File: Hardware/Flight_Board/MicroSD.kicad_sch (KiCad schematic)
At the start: 14 parts, among them J5 MEM2067-02-180-00-A_REVB

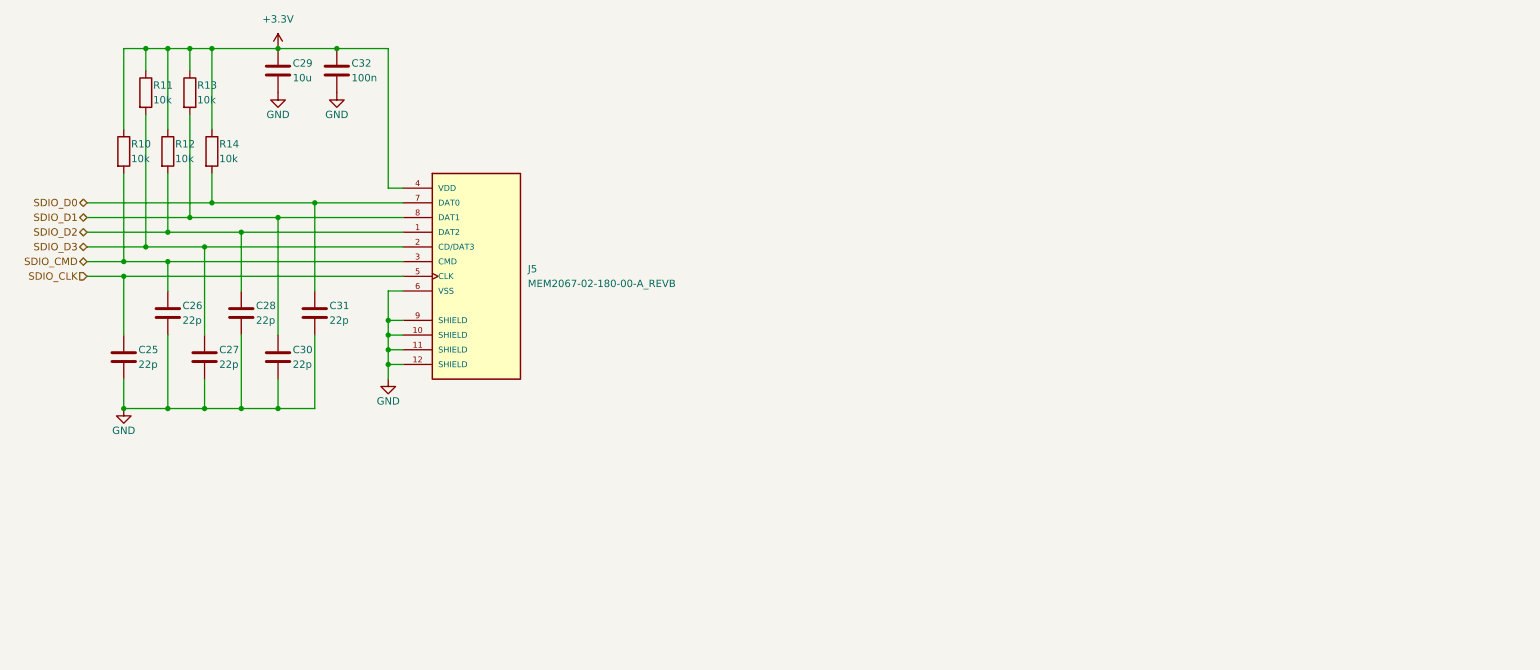
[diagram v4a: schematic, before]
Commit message: Add LEDs and test points
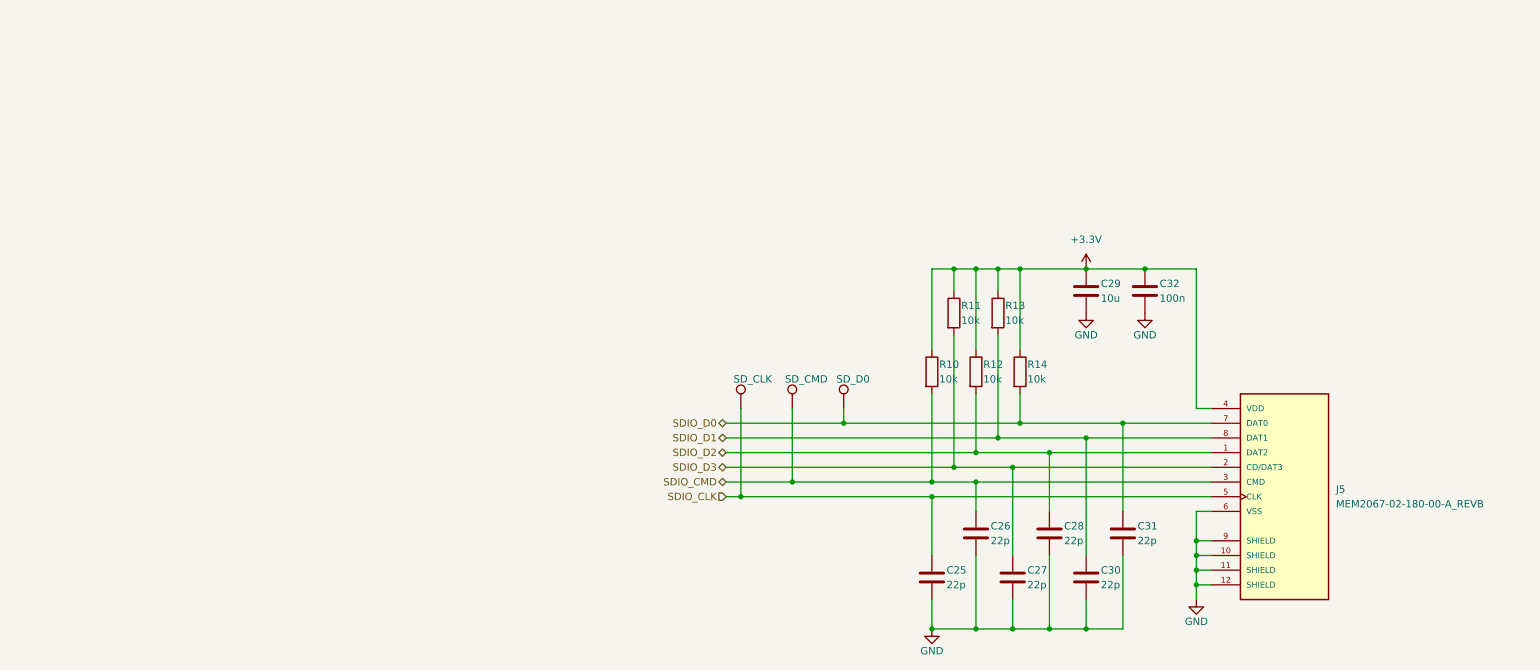
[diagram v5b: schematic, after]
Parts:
- added TP2: SD_D0, symbol Connector:TestPoint
- added TP2: SD_CLK, symbol Connector:TestPoint
- added TP2: SD_CMD, symbol Connector:TestPoint
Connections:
- net SDIO_CLK: now also TP2.1
- net SDIO_CMD: now also TP2.1
- net SDIO_D0: now also TP2.1
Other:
- moved on the sheet: C25, C26, C27, C28, C29, C30, C31, C32, J5, R10, R11, R12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

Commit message: final touches, bom, footprints
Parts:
- C25, C26, C27, C28, C29, C30, C31, C32: footprint (none) -> Capacitor_SMD:C_0603_1608Metric_Pad1.08x0.95mm_HandSolder
- R10, R11, R12, R13, R14: footprint (none) -> Resistor_SMD:R_0603_1608Metric_Pad0.98x0.95mm_HandSolder
- TP2: footprint (none) -> TestPoint:TestPoint_THTPad_2.0x2.0mm_Drill1.0mm
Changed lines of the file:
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@@
       (effects (font (size 1.27 1.27)) (justify left))
     )
-    (property "Footprint" "" (at 215.392 97.79 90)
+    (property "Footprint" "Resistor_SMD:R_0603_1608Metric_Pad0.98x0.95mm_HandSolder" (at 215.392 97.79 90)
       (effects (font (size 1.27 1.27)) hide)
     )
@@
       (effects (font (size 1.27 1.27)) (justify left))
     )
-    (property "Footprint" "" (at 203.962 87.63 90)
+    (property "Footprint" "Resistor_SMD:R_0603_1608Metric_Pad0.98x0.95mm_HandSolder" (at 203.962 87.63 90)
       (effects (font (size 1.27 1.27)) hide)
     )
@@
       (effects (font (size 1.27 1.27)) (justify left))
     )
-    (property "Footprint" "" (at 207.772 97.79 90)
+    (property "Footprint" "Resistor_SMD:R_0603_1608Metric_Pad0.98x0.95mm_HandSolder" (at 207.772 97.79 90)
       (effects (font (size 1.27 1.27)) hide)
     )
@@
       (effects (font (size 1.27 1.27)) (justify left))
     )
-    (property "Footprint" "" (at 229.5652 137.16 0)
+    (property "Footprint" "Capacitor_SMD:C_0603_1608Metric_Pad1.08x0.95mm_HandSolder" (at 229.5652 137.16 0)
       (effects (font (size 1.27 1.27)) hide)
     )
@@
       (effects (font (size 1.27 1.27)) (justify left))
     )
-    (property "Footprint" "" (at 239.7252 87.63 0)
+    (property "Footprint" "Capacitor_SMD:C_0603_1608Metric_Pad1.08x0.95mm_HandSolder" (at 239.7252 87.63 0)
       (effects (font (size 1.27 1.27)) hide)
     )
@@
       (effects (font (size 1.27 1.27)) (justify left))
     )
-    (property "Footprint" "" (at 191.77 104.14 0)
+    (property "Footprint" "TestPoint:TestPoint_THTPad_2.0x2.0mm_Drill1.0mm" (at 191.77 104.14 0)
       (effects (font (size 1.27 1.27)) hide)
     )
@@
       (effects (font (size 1.27 1.27)) (justify left))
     )
-    (property "Footprint" "" (at 173.99 104.14 0)
+    (property "Footprint" "TestPoint:TestPoint_THTPad_2.0x2.0mm_Drill1.0mm" (at 173.99 104.14 0)
       (effects (font (size 1.27 1.27)) hide)
     )
@@
       (effects (font (size 1.27 1.27)) (justify left))
     )
-    (property "Footprint" "" (at 211.582 87.63 90)
+    (property "Footprint" "Resistor_SMD:R_0603_1608Metric_Pad0.98x0.95mm_HandSolder" (at 211.582 87.63 90)
       (effects (font (size 1.27 1.27)) hide)
     )
@@
       (effects (font (size 1.27 1.27)) (justify left))
     )
-    (property "Footprint" "" (at 216.8652 137.16 0)
+    (property "Footprint" "Capacitor_SMD:C_0603_1608Metric_Pad1.08x0.95mm_HandSolder" (at 216.8652 137.16 0)
       (effects (font (size 1.27 1.27)) hide)
     )
@@
       (effects (font (size 1.27 1.27)) (justify left))
     )
-    (property "Footprint" "" (at 235.9152 129.54 0)
+    (property "Footprint" "Capacitor_SMD:C_0603_1608Metric_Pad1.08x0.95mm_HandSolder" (at 235.9152 129.54 0)
       (effects (font (size 1.27 1.27)) hide)
     )
@@
       (effects (font (size 1.27 1.27)) (justify left))
     )
-    (property "Footprint" "" (at 223.2152 129.54 0)
+    (property "Footprint" "Capacitor_SMD:C_0603_1608Metric_Pad1.08x0.95mm_HandSolder" (at 223.2152 129.54 0)
       (effects (font (size 1.27 1.27)) hide)
     )
@@
       (effects (font (size 1.27 1.27)) (justify left))
     )
-    (property "Footprint" "" (at 229.5652 87.63 0)
+    (property "Footprint" "Capacitor_SMD:C_0603_1608Metric_Pad1.08x0.95mm_HandSolder" (at 229.5652 87.63 0)
       (effects (font (size 1.27 1.27)) hide)
     )
@@
       (effects (font (size 1.27 1.27)) (justify left))
     )
-    (property "Footprint" "" (at 200.152 97.79 90)
+    (property "Footprint" "Resistor_SMD:R_0603_1608Metric_Pad0.98x0.95mm_HandSolder" (at 200.152 97.79 90)
       (effects (font (size 1.27 1.27)) hide)
     )
@@
       (effects (font (size 1.27 1.27)) (justify left))
     )
-    (property "Footprint" "" (at 202.8952 137.16 0)
+    (property "Footprint" "Capacitor_SMD:C_0603_1608Metric_Pad1.08x0.95mm_HandSolder" (at 202.8952 137.16 0)
       (effects (font (size 1.27 1.27)) hide)
     )
@@
       (effects (font (size 1.27 1.27)) (justify left))
     )
-    (property "Footprint" "" (at 210.5152 129.54 0)
+    (property "Footprint" "Capacitor_SMD:C_0603_1608Metric_Pad1.08x0.95mm_HandSolder" (at 210.5152 129.54 0)
       (effects (font (size 1.27 1.27)) hide)
     )
@@
       (effects (font (size 1.27 1.27)) (justify left))
     )
-    (property "Footprint" "" (at 182.88 104.14 0)
-      (effects (font (size 1.27 1.27)) hide)
-    )
+    (property "Footprint" "TestPoint:TestPoint_THTPad_2.0x2.0mm_Drill1.0mm" (at 182.88 104.14 0)
+      (effects (font (size 1.27 1.27)) hide)
+    )

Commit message: fix some stuff and begin layout grouping
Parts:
- J5: footprint MEM2067-02-180-00-A_REVB:GCT_MEM2067-02-180-00-A_REVB -> Project:GCT_MEM2067-02-180-00-A_REVB
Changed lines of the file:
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@@
       (effects (font (size 1.27 1.27)) (justify left))
     )
-    (property "Footprint" "MEM2067-02-180-00-A_REVB:GCT_MEM2067-02-180-00-A_REVB" (at 261.62 142.24 0)
+    (property "Footprint" "Project:GCT_MEM2067-02-180-00-A_REVB" (at 261.62 142.24 0)
       (effects (font (size 1.27 1.27)) (justify bottom) hide)
     )

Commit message: initial route of 4-layer board
ouch
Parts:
- renumbered C25 to C23, C26 to C24, C27 to C25, C28 to C26, C29 to C27, C30 to C28, C31 to C29, C32 to C30, R10 to R13, R11 to R14, R12 to R15, R13 to R16, R14 to R17
